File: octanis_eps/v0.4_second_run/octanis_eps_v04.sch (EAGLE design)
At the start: 107 parts, among them IC1 OPA2333DGK, IC5 OPA2333DGK, IC7 OPA2333DGK, IC9 OPA2333DGK, Q1 FC-12M, Q2 N-HEXFET-2D_SOT232-, Q3 N-HEXFET-2D_SOT232-, Q4 N-HEXFET-2D_SOT232-

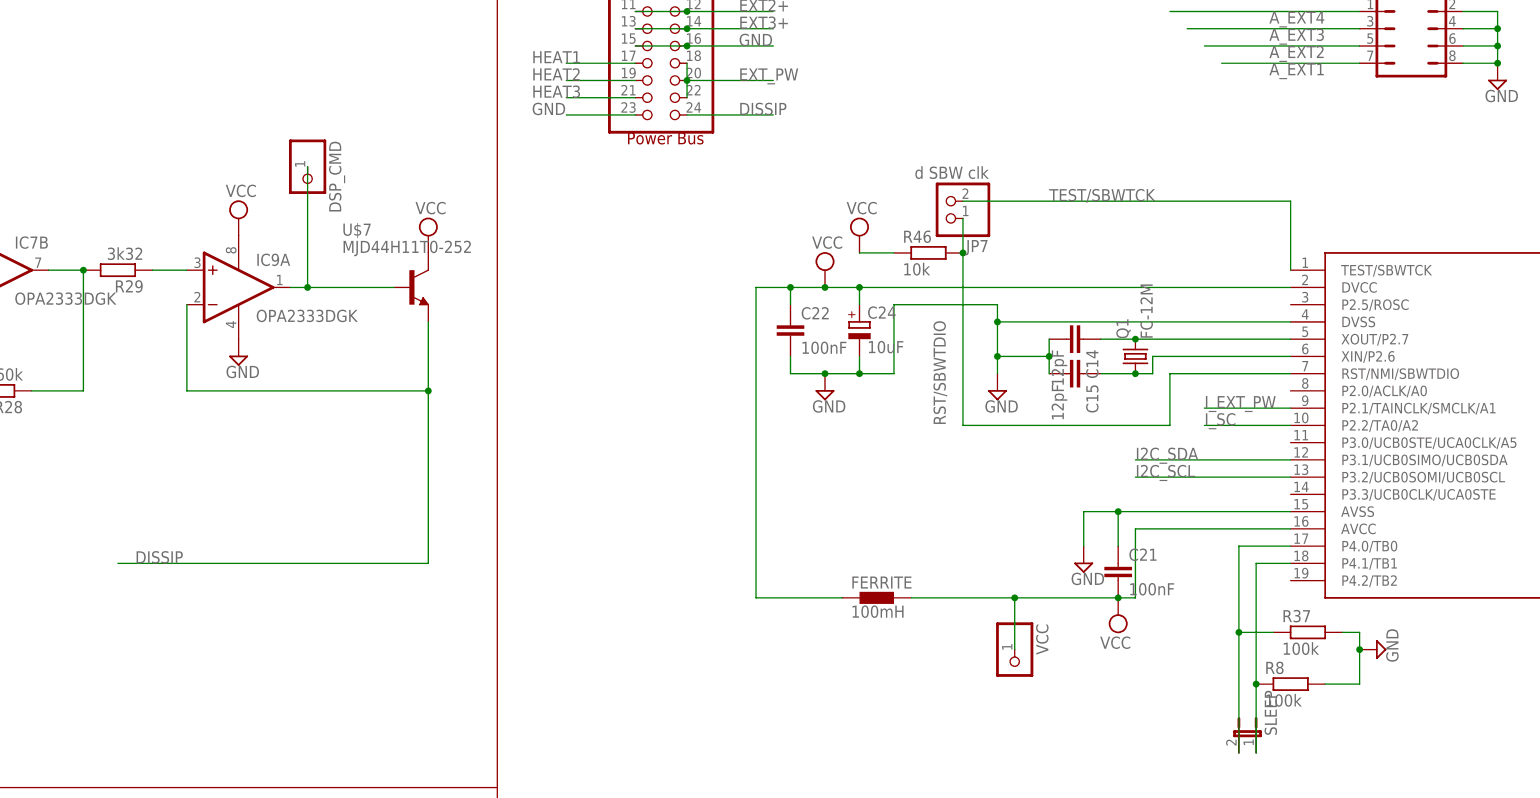
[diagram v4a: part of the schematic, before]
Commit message: changed IC9A=OPA2333 (2ch) for IC9=0PA347 with SC70-5 small outline package. OPA347 allows for bigger driving currents so to be able to drive the POWER N-FET on disispation CMD (cf bgeissma for details), modifications still to be performed on the boost converter circuit
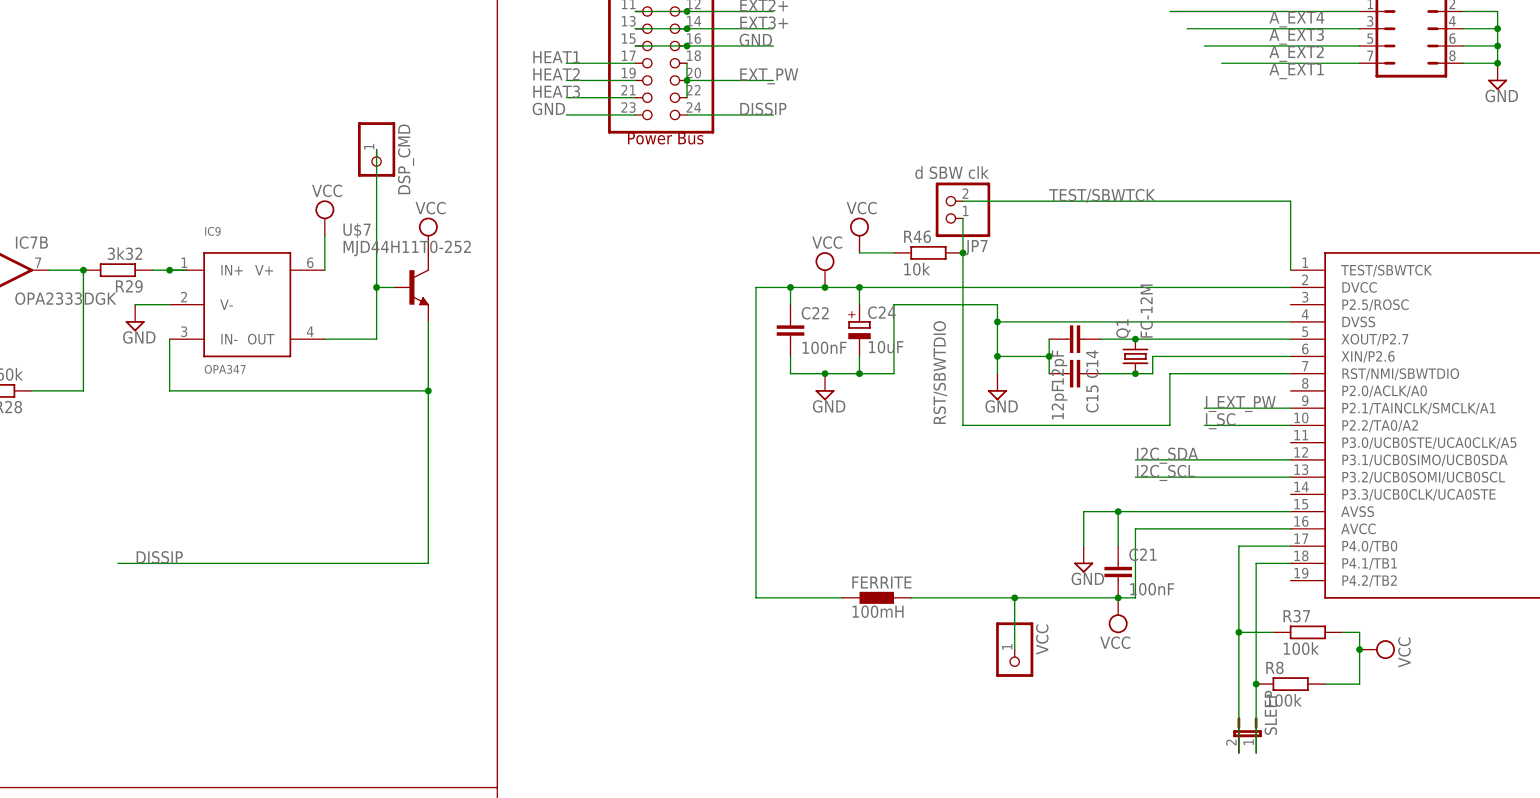
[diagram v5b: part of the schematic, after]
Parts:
- IC9: value OPA2333DGK -> OPA347; device linear:OPA2333DGK -> Octanis1_EPS:OPA347
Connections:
- net N$27 renamed TB1
- net N$36 renamed TB0
- net DISSIP: now also IC9.IN-; no longer IC9A.-IN
- net GND: now also IC9.V-; no longer IC9P.V-, R37.2, R8.2
- net N$22: now also IC9.IN+; no longer IC9A.+IN
- net N$45: now also IC9.OUT; no longer IC9A.OUT
- net VCC: now also IC9.V+, R37.2, R8.2; no longer IC9P.V+
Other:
- moved on the sheet: DSP_CMD
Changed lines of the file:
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@@
 <part name="SUPPLY32" library="supply2" deviceset="GND" device=""/>
 <part name="IC7" library="linear" deviceset="OPA2333" device="DGK"/>
-<part name="IC9" library="linear" deviceset="OPA2333" device="DGK"/>
 <part name="C_IC9" library="rcl" deviceset="C-EU" device="C0603" value="100nF"/>
 <part name="SUPPLY33" library="supply2" deviceset="VCC" device=""/>
@@
 <part name="R8" library="rcl" deviceset="R-EU_" device="R0603" value="100k"/>
 <part name="R37" library="rcl" deviceset="R-EU_" device="R0603" value="100k"/>
-<part name="SUPPLY60" library="supply2" deviceset="GND" device=""/>
+<part name="SUPPLY60" library="supply2" deviceset="VCC" device=""/>
+<part name="IC9" library="Octanis1_EPS" deviceset="OPA347" device=""/>
 </parts>
 <sheets>
@@
 <instance part="IC7" gate="B" x="139.7" y="45.72"/>
 <instance part="IC7" gate="P" x="2.54" y="-198.12"/>
-<instance part="IC9" gate="A" x="175.26" y="43.18"/>
 <instance part="C_IC9" gate="G$1" x="106.68" y="-17.78" rot="R180"/>
 <instance part="SUPPLY33" gate="G$1" x="106.68" y="-7.62"/>
@@
 <instance part="SUPPLY44" gate="GND" x="312.42" y="-180.34"/>
 <instance part="SUPPLY45" gate="G$1" x="383.54" y="-160.02"/>
-<instance part="IC9" gate="P" x="175.26" y="43.18"/>
-<instance part="SUPPLY46" gate="G$1" x="175.26" y="53.34"/>
-<instance part="SUPPLY47" gate="GND" x="175.26" y="33.02"/>
+<instance part="SUPPLY46" gate="G$1" x="187.96" y="53.34"/>
+<instance part="SUPPLY47" gate="GND" x="160.02" y="38.1"/>
 <instance part="0.47UH" gate="G$1" x="355.6" y="-162.56"/>
 <instance part="10UH" gate="G$1" x="124.46" y="-157.48"/>
@@
 <instance part="RSENSE3" gate="G$1" x="-35.56" y="-205.74" rot="R270"/>
 <instance part="BT_CHG" gate="G$1" x="187.96" y="-149.86" rot="R270"/>
-<instance part="DSP_CMD" gate="G$1" x="185.42" y="58.42" rot="R270"/>
+<instance part="DSP_CMD" gate="G$1" x="195.58" y="60.96" rot="R270"/>
 <instance part="JP2" gate="B" x="347.98" y="81.28" rot="R270"/>
 <instance part="SUPPLY57" gate="GND" x="360.68" y="73.66"/>
@@
 <instance part="R8" gate="G$1" x="330.2" y="-15.24"/>
 <instance part="R37" gate="G$1" x="332.74" y="-7.62"/>
-<instance part="SUPPLY60" gate="GND" x="342.9" y="-10.16" rot="R90"/>
+<instance part="SUPPLY60" gate="G$1" x="342.9" y="-10.16" rot="R270"/>
+<instance part="IC9" gate="G$1" x="175.26" y="40.64"/>
 </instances>
 <busses>
@@
 </segment>
 <segment>
-<pinref part="IC9" gate="P" pin="V-"/>
-<pinref part="SUPPLY47" gate="GND" pin="GND"/>
-</segment>
-<segment>
 <pinref part="JP1" gate="A" pin="3"/>
 <pinref part="JP1" gate="A" pin="4"/>
@@
 </segment>
 <segment>
-<pinref part="R37" gate="G$1" pin="2"/>
-<wire x1="337.82" y1="-7.62" x2="340.36" y2="-7.62" width="0.1524" layer="91"/>
-<pinref part="SUPPLY60" gate="GND" pin="GND"/>
-<wire x1="340.36" y1="-7.62" x2="340.36" y2="-10.16" width="0.1524" layer="91"/>
-<wire x1="340.36" y1="-10.16" x2="340.36" y2="-15.24" width="0.1524" layer="91"/>
-<junction x="340.36" y="-10.16"/>
-<pinref part="R8" gate="G$1" pin="2"/>
-<wire x1="340.36" y1="-15.24" x2="335.28" y2="-15.24" width="0.1524" layer="91"/>
+<pinref part="SUPPLY47" gate="GND" pin="GND"/>
+<pinref part="IC9" gate="G$1" pin="V-"/>
+<wire x1="160.02" y1="40.64" x2="165.1" y2="40.64" width="0.1524" layer="91"/>
 </segment>
 </net>
@@
 </segment>
 <segment>
-<pinref part="IC9" gate="P" pin="V+"/>
-<pinref part="SUPPLY46" gate="G$1" pin="VCC"/>
-</segment>
-<segment>
 <pinref part="U$6" gate="G$1" pin="AVCC"/>
 <wire x1="330.2" y1="7.62" x2="307.34" y2="7.62" width="0.1524" layer="91"/>
@@
 <pinref part="SUPPLY56" gate="G$1" pin="VCC"/>
 </segment>
+<segment>
+<pinref part="R37" gate="G$1" pin="2"/>
+<wire x1="337.82" y1="-7.62" x2="340.36" y2="-7.62" width="0.1524" layer="91"/>
+<wire x1="340.36" y1="-7.62" x2="340.36" y2="-10.16" width="0.1524" layer="91"/>
+<pinref part="R8" gate="G$1" pin="2"/>
+<wire x1="340.36" y1="-10.16" x2="340.36" y2="-15.24" width="0.1524" layer="91"/>
+<wire x1="340.36" y1="-15.24" x2="335.28" y2="-15.24" width="0.1524" layer="91"/>
+<pinref part="SUPPLY60" gate="G$1" pin="VCC"/>
+<junction x="340.36" y="-10.16"/>
+</segment>
+<segment>
+<pinref part="IC9" gate="G$1" pin="V+"/>
+<pinref part="SUPPLY46" gate="G$1" pin="VCC"/>
+<wire x1="187.96" y1="50.8" x2="187.96" y2="45.72" width="0.1524" layer="91"/>
+</segment>
 </net>
 <net name="VREF" class="0">
@@
 <net name="N$22" class="0">
 <segment>
-<pinref part="IC9" gate="A" pin="+IN"/>
 <pinref part="R29" gate="G$1" pin="1"/>
-<wire x1="167.64" y1="45.72" x2="162.56" y2="45.72" width="0.1524" layer="91"/>
+<wire x1="167.64" y1="45.72" x2="165.1" y2="45.72" width="0.1524" layer="91"/>
+<pinref part="IC9" gate="G$1" pin="IN+"/>
+<wire x1="165.1" y1="45.72" x2="162.56" y2="45.72" width="0.1524" layer="91"/>
+<junction x="165.1" y="45.72"/>
 </segment>
 </net>
@@
 <segment>
 <pinref part="U$7" gate="G$1" pin="B"/>
-<pinref part="IC9" gate="A" pin="OUT"/>
-<wire x1="198.12" y1="43.18" x2="185.42" y2="43.18" width="0.1524" layer="91"/>
+<wire x1="198.12" y1="43.18" x2="195.58" y2="43.18" width="0.1524" layer="91"/>
 <pinref part="DSP_CMD" gate="G$1" pin="1"/>
-<wire x1="185.42" y1="43.18" x2="182.88" y2="43.18" width="0.1524" layer="91"/>
-<wire x1="185.42" y1="60.96" x2="185.42" y2="43.18" width="0.1524" layer="91"/>
-<junction x="185.42" y="43.18"/>
+<wire x1="195.58" y1="63.5" x2="195.58" y2="43.18" width="0.1524" layer="91"/>
+<pinref part="IC9" gate="G$1" pin="OUT"/>
+<wire x1="187.96" y1="35.56" x2="195.58" y2="35.56" width="0.1524" layer="91"/>
+<wire x1="195.58" y1="35.56" x2="195.58" y2="43.18" width="0.1524" layer="91"/>
+<junction x="195.58" y="43.18"/>
 </segment>
 </net>
@@
 <wire x1="203.2" y1="2.54" x2="157.48" y2="2.54" width="0.1524" layer="91"/>
 <label x="160.02" y="2.54" size="1.778" layer="95"/>
-<pinref part="IC9" gate="A" pin="-IN"/>
-<wire x1="167.64" y1="27.94" x2="167.64" y2="40.64" width="0.1524" layer="91"/>
+<wire x1="165.1" y1="27.94" x2="165.1" y2="35.56" width="0.1524" layer="91"/>
 <pinref part="U$7" gate="G$1" pin="E"/>
 <wire x1="203.2" y1="38.1" x2="203.2" y2="27.94" width="0.1524" layer="91"/>
-<wire x1="167.64" y1="27.94" x2="203.2" y2="27.94" width="0.1524" layer="91"/>
+<wire x1="165.1" y1="27.94" x2="203.2" y2="27.94" width="0.1524" layer="91"/>
 <junction x="203.2" y="27.94"/>
+<pinref part="IC9" gate="G$1" pin="IN-"/>
 </segment>
 <segment>
@@
 </segment>
 </net>
-<net name="N$27" class="0">
+<net name="TB1" class="0">
 <segment>
 <pinref part="U$6" gate="G$1" pin="P4.1/TB1"/>
@@
 </segment>
 </net>
-<net name="N$36" class="0">
+<net name="TB0" class="0">
 <segment>
 <pinref part="U$6" gate="G$1" pin="P4.0/TB0"/>

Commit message: re-routed EPS. adapted silkscreen on EPS
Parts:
- removed C15: 12pF, rcl:C-EUC0603
- removed C21, C_IC5: 100nF, rcl:C-EUC0603
- removed IC5: OPA2333DGK, linear:OPA2333DGK
- removed JP7: d SBW clk, pinhead:PINHD-1X2
- removed R30: 20k, rcl:R-EU_R0603
- removed R31: 23.2k, rcl:R-EU_R0603
- removed R32: 82k, rcl:R-EU_R0603
- removed R33, R42, R43, R44: 1M, rcl:R-EU_R0603
- removed R34, R35, R36: 162k, rcl:R-EU_R0603
- removed R38, R39, R46: 10k, rcl:R-EU_R0603
- removed R40: 920k, rcl:R-EU_R0603
- removed R45: 0Ohm, rcl:R-EU_R0603
- removed RSENSE3: RSENSE3, Octanis1_EPS:CURRENT_RESISTOR
- removed U$10: MBRM120LTIG, Octanis1_EPS:MBRM120LTIG
- added C12: 1.5uF, rcl:C-EUC0603
- added C13: 4.7u, rcl:C-EUC1206
- added C_IC2: 100nF, rcl:C-EUC0603
- added IC2: OPA2333DGK, linear:OPA2333DGK
- added JP3: (no value), jumper:JP4Q
- added R100: 953, rcl:R-EU_R0603
- added R101: 86k6, rcl:R-EU_R0603
- added R102: 4k02, rcl:R-EU_R0603
- added R103, R107, R116, R118: 200k, rcl:R-EU_R0603
- added R104, R108, R112, R117, R119: 100k, rcl:R-EU_R0603
- added R105: 147k, rcl:R-EU_R0603
- added R106: 3k32, rcl:R-EU_R0603
- added R109: 560k, rcl:R-EU_R0603
- added RSENSE1: RSENSE2, Octanis1_EPS:CURRENT_RESISTOR
- added U$100: MAX6190BESA, Octanis1_EPS:MAX6190BESA
- C1: value 10nF -> 1.5uF
- C10: value 22u -> 100nF; device rcl:C-EUC1206 -> rcl:C-EUC0603
- C11: value 4.7p -> 10nF
- C14: value 12pF -> 22u
- C3: value 1.5uF -> 10u; device rcl:C-EUC0603 -> rcl:C-EUC1206
- C4: value 4.7u -> 22u
- C5: value 470p -> 12pF
- C6: value 1.5uF -> 12pF
- C8: value 22u -> 4.7p
- C9: value 10u -> 470p; device rcl:C-EUC1206 -> rcl:C-EUC0603
- JP2: value (none) -> d SBW clk; device jumper:JP4Q -> pinhead:PINHD-1X2
- Q1: value FC-12M -> N-HEXFET-2D_SOT232-; device crystal:FC-12M -> transistor-power:N-HEXFET-2D_SOT232-
- Q3: value N-HEXFET-2D_SOT232- -> FC-12M; device transistor-power:N-HEXFET-2D_SOT232- -> crystal:FC-12M
- R10: value 30.1k -> 1k
- R11, R18, R23: value 100k -> 10k
- R12: value 200k -> 82k
- R13: value 1M -> 1k
- R14, R22: value 200k -> 162k
- R16: value 1k -> 30.1k
- R17: value 200k -> 1k
- R19: value 200k -> 100k
- R20: value 100k -> 920k
- R21: value 1k -> 560k
- R24: value 147k -> 1M
- R25: value 953 -> 20k
- R26: value 86k6 -> 31.60k
- R27: value 4k02 -> 162k
- R28: value 560k -> 23.2k
- R29: value 3k32 -> 200k
- R4: value 560k -> 0Ohm
- R5: value 31.60k -> 1k
- R6, R8: value 100k -> 1M
- R7, R9: value 1k -> 1M
- RSENSE2: value RSENSE2 -> RSENSE3
- U$1: value MAX6190BESA -> MJD44H11T0-252; device Octanis1_EPS:MAX6190BESA -> Octanis1_EPS:MJD44H11T0-252
- U$4: value LTC3402 -> TPS62086; device Octanis1_EPS:LTC3402 -> Octanis1_EPS:TPS62086
- U$5: value TPS62086 -> MSP430G2544; device Octanis1_EPS:TPS62086 -> Octanis1_EPS:MSP430G2544
- U$6: value MSP430G2544 -> LTC3402; device Octanis1_EPS:MSP430G2544 -> Octanis1_EPS:LTC3402
- U$7: value MJD44H11T0-252 -> MBRM120LTIG; device Octanis1_EPS:MJD44H11T0-252 -> Octanis1_EPS:MBRM120LTIG
- renumbered C22 to C102, C24 to C103, C26 to C104, C27 to C100, C28 to C101, C29 to C105, C_IC7 to C_IC100, C_IC9 to C_IC101, IC7 to IC100, IC9 to IC101, Q4 to Q100, R37 to R111, R41 to R110, R79 to R113, R80 to R114, R81 to R115, U$16 to U$103, U$17 to U$102, U$18 to U$101
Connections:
- net A_EXT1: now also JP3.7, U$5.P4.3/TB0/A12; no longer JP2.7, U$6.P4.3/TB0/A12
- net A_EXT2: now also JP3.5, U$5.P4.4/TB1/A13; no longer JP2.5, U$6.P4.4/TB1/A13
- net A_EXT3: now also JP3.3, U$5.P4.5/TB2/A14; no longer JP2.3, U$6.P4.5/TB2/A14
- net A_EXT4: now also JP3.1, U$5.P4.6/TBOUTH/A15; no longer JP2.1, U$6.P4.6/TBOUTH/A15
- net BT+: now also C3.2, R116.2, R4.1, RSENSE2.V1, U$4.VIN; no longer C9.2, R19.2, R45.1, RSENSE3.V1, U$5.VIN
- net BT_CHG: now also C14.2, R29.1, RSENSE2.V2, U$6.VOUT, U$7.K; no longer C8.2, R12.1, RSENSE3.V2, U$10.K, U$4.VOUT
- net CHG_CMD: now also C11.1, IC2B.OUT, R14.2, R21.2; no longer C1.1, IC1B.OUT, R34.2, R4.2
- net DISSIP: now also U$1.E; no longer U$7.E
- net EN_CHG: now also R15.1, U$5.P1.4/SMCLK/TCK, U$6.SHDN; no longer R6.1, U$4.SHDN, U$6.P1.4/SMCLK/TCK
- net EN_EXT1: now also U$5.P1.5/TA0/TMS; no longer U$6.P1.5/TA0/TMS
- net EN_EXT2: now also U$5.P1.6/TA1/TDI; no longer U$6.P1.6/TA1/TDI
- net EN_EXT3: now also U$5.P1.7/TA2/TDO/TDI; no longer U$6.P1.7/TA2/TDO/TDI
- net EN_HEAT1: now also R5.2, R8.1, U$5.P1.1/TA0; no longer R1.2, R42.1, U$6.P1.1/TA0
- net EN_HEAT2: now also R3.2, R9.1, U$5.P1.2/TA1; no longer R2.2, R43.1, U$6.P1.2/TA1
- net EN_HEAT3: now also R10.2, R7.1, U$5.P1.3/TA2; no longer R3.2, R44.1, U$6.P1.3/TA2
- net GND: now also C1.1, C12.1, C13.1, C14.1, C5.2, C6.2, C_IC2.1, IC2P.V-, JP3.2, JP3.4, JP3.6, JP3.8, Q1.S, R101.2, R104.1, R107.2, R117.1, R118.2, R12.2, R15.2, R16.2, R19.1, R25.2, R7.2, R8.2, R9.2, U$100.GND, U$5.AVSS, U$5.DVSS, U$6.GND, U$6.MODE; no longer C11.1, C14.2, C15.2, C21.1, C6.1, C9.1, C_IC5.1, IC5P.V-, JP2.2, JP2.4, JP2.6, JP2.8, Q3.S, R10.2, R11.1, R15.1, R17.2, R20.1, R22.2, R26.2, R30.2, R32.2, R42.2, R43.2, R44.2, R6.2, U$1.GND, U$4.MODE, U$5.GND, U$6.AVSS, U$6.DVSS
- net HEAT2: now also Q1.D; no longer Q3.D
- net I2C_SCL: now also U$5.P3.2/UCB0SOMI/UCB0SCL; no longer U$6.P3.2/UCB0SOMI/UCB0SCL
- net I2C_SDA: now also U$5.P3.1/UCB0SIMO/UCB0SDA; no longer U$6.P3.1/UCB0SIMO/UCB0SDA
- net I_EXT_PW: now also C1.2, R1.1, U$5.P2.1/TAINCLK/SMCLK/A1; no longer C2.2, R7.1, U$6.P2.1/TAINCLK/SMCLK/A1
- net I_SC: now also C2.2, R2.1, U$5.P2.2/TA0/A2; no longer C3.2, R9.1, U$6.P2.2/TA0/A2
- net N$1: now also R1.2, U$3.OUT; no longer R7.2, U$2.OUT
- net N$10: now also IC1B.OUT, R119.1, R13.2; no longer IC5B.OUT, R21.2, R23.1
- net N$11: now also C11.2, IC2B.-IN, R14.1, R22.2, R27.2; no longer C1.2, IC1B.-IN, R34.1, R35.2, R36.2
- net N$12: now also IC1A.OUT, R108.1, R17.2; no longer IC5A.OUT, R16.2, R18.1
- net N$13: now also IC1A.-IN, R107.1, R108.2; no longer IC5A.-IN, R17.1, R18.2
- net N$14: now also IC1A.+IN, R103.1, R104.2; no longer IC5A.+IN, R14.1, R15.2
- net N$15: now also IC1B.-IN, R118.1, R119.2; no longer IC5B.-IN, R22.1, R23.2
- net N$16: now also IC1B.+IN, R116.1, R117.2; no longer IC5B.+IN, R19.1, R20.2
- net N$17: now also R23.2; no longer R38.2
- net N$18: now also R100.1, R105.2; no longer R24.2, R25.1
- net N$19: now also R100.2, R101.1; no longer R25.2, R26.1
- net N$2: now also R2.2, U$2.OUT; no longer R9.2, U$3.OUT
- net N$20: now also R102.1, R109.2; no longer R27.1, R28.2
- net N$21: now also R106.2, R109.1; no longer R28.1, R29.2
- net N$22: now also R106.1; no longer R29.1
- net N$23: now also R19.2, R21.1, R29.2, U$6.FB; no longer R11.2, R12.2, R4.1, U$4.FB
- net N$24: now also U$6.SW, U$7.A; no longer U$10.A, U$4.SW
- net N$25: now also R6.2, U$4.PG; no longer R13.2, U$5.PG
- net N$26: now also U$4.SW; no longer U$5.SW
- net N$28: now also R18.2, R20.1; no longer R39.2, R40.1
- net N$29: now also R5.1; no longer R1.1
- net N$3: now also R16.1, U$6.RT; no longer R10.1, U$4.RT
- net N$30: now also R4.2, U$4.EN; no longer R45.2, U$5.EN
- net N$31: now also Q1.G, R3.1; no longer Q3.G, R2.1
- net N$32: now also U$3.IN+; no longer U$2.IN+
- net N$33: now also U$3.IN-; no longer U$2.IN-
- net N$34: now also RSENSE1.V1, U$2.IN+; no longer RSENSE2.V1, U$3.IN+
- net N$35: now also RSENSE1.V2, U$2.IN-; no longer RSENSE2.V2, U$3.IN-
- net N$37: now also R10.1; no longer R3.1
- net N$38: now also R23.1, RSENSE2.I2; no longer R38.1, RSENSE3.I2
- net N$4: now also C9.1, R12.1; no longer C5.1, R32.1
- net N$40: now also R18.1, RSENSE2.I1; no longer R39.1, RSENSE3.I1
- net N$45: now also U$1.B; no longer U$7.B
- net N$48: now also C5.1, Q3.2, U$5.XOUT/P2.7; no longer C14.1, Q1.2, U$6.XOUT/P2.7
- net N$5: now also R22.1; no longer R36.1
- net N$50: now also C6.1, Q3.1, U$5.XIN/P2.6; no longer C15.1, Q1.1, U$6.XIN/P2.6
- net N$6: now also IC2A.+IN, R25.1, R26.2; no longer IC1A.+IN, R30.1, R5.2
- net N$7: now also IC2A.-IN, R24.1, R28.1; no longer IC1A.-IN, R31.1, R33.1
- net N$8: now also C8.2, C9.2, U$6.VC; no longer C11.2, C5.2, U$4.VC
- net N$9: now also IC2A.OUT, R24.2, R27.1; no longer IC1A.OUT, R33.2, R35.1
- net RST/SBWTDIO: now also JP2.1, R11.2, U$5.RST/NMI/SBWTDIO; no longer JP7.1, R46.2, U$6.RST/NMI/SBWTDIO
- net SC+: now also RSENSE1.I1; no longer RSENSE2.I1
- net TB0: now also U$5.P4.0/TB0; no longer U$6.P4.0/TB0
- net TB1: now also R112.1, U$5.P4.1/TB1; no longer R8.1, U$6.P4.1/TB1
- net TEST/SBWTCK: now also JP2.2, U$5.TEST/SBWTCK; no longer JP7.2, U$6.TEST/SBWTCK
- net VCC: now also C13.2, C_IC2.2, IC2P.V+, R103.2, R105.1, R11.1, R112.2, R26.1, R6.1, RSENSE1.I2, U$1.C, U$100.NC2, U$4.FB, U$4.VOS, U$5.AVCC, U$5.DVCC, U$6.VIN; no longer C21.2, C_IC5.2, IC5P.V+, R13.1, R14.2, R24.1, R46.1, R5.1, R8.2, RSENSE2.I2, U$1.NC2, U$4.VIN, U$5.FB, U$5.VOS, U$6.AVCC, U$6.DVCC, U$7.C
- net VREF: now also IC2B.+IN, R102.2, R20.2, R28.2, U$100.OUT; no longer IC1B.+IN, R27.2, R31.2, R40.2, U$1.OUT
- net V_BT_MS: now also R13.1, U$5.P3.7/A7; no longer R21.1, U$6.P3.7/A7
- net V_BUS_MS: now also C12.2, R17.1, U$5.P3.6/A6; no longer C6.2, R16.1, U$6.P3.6/A6
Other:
- moved on the sheet: C1, C10, C11, C14, C2, C3, C4, C5, C6, C8, C9, C_IC1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
